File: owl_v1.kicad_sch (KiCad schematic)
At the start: 17 parts, among them SW1 SW_SPDT, U1 STM32F103C8T6, Y1 8MHz, Y2 32k768

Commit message: [feat] Initial routing for the owl PCB
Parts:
- C14, C16: footprint Capacitor_SMD:C_0402_1005Metric -> Capacitor_SMD:C_0603_1608Metric
- L1: footprint Inductor_SMD:L_0402_1005Metric -> Inductor_SMD:L_0603_1608Metric
- SW1: footprint (none) -> Button_Switch_SMD:SW_SPDT_CK_JS102011SAQN
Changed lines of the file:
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@@
 	(wire
 		(pts
+			(xy 46.99 63.5) (xy 48.26 63.5)
+		)
+		(stroke
+			(width 0)
+			(type default)
+		)
+	)
+	(wire
+		(pts
 			(xy 113.03 167.64) (xy 119.38 167.64)
 		)
@@
 	(wire
 		(pts
-			(xy 46.99 63.5) (xy 46.99 67.31)
+			(xy 182.88 104.14) (xy 185.42 104.14)
 		)
 		(stroke
@@
 	(wire
 		(pts
-			(xy 182.88 104.14) (xy 185.42 104.14)
+			(xy 45.72 63.5) (xy 46.99 63.5)
 		)
 		(stroke
@@
 	(wire
 		(pts
-			(xy 48.26 63.5) (xy 46.99 63.5)
+			(xy 64.77 194.31) (xy 71.12 194.31)
 		)
 		(stroke
@@
 	(wire
 		(pts
-			(xy 64.77 194.31) (xy 71.12 194.31)
+			(xy 182.88 78.74) (xy 185.42 78.74)
 		)
 		(stroke
@@
 	(wire
 		(pts
-			(xy 182.88 78.74) (xy 185.42 78.74)
+			(xy 49.53 31.75) (xy 52.07 31.75)
 		)
 		(stroke
@@
 	(wire
 		(pts
-			(xy 49.53 31.75) (xy 52.07 31.75)
+			(xy 238.76 99.06) (xy 242.57 99.06)
 		)
 		(stroke
@@
 	(wire
 		(pts
-			(xy 238.76 99.06) (xy 242.57 99.06)
+			(xy 46.99 63.5) (xy 46.99 67.31)
 		)
 		(stroke
@@
 	(wire
 		(pts
-			(xy 45.72 63.5) (xy 46.99 63.5)
-		)
-		(stroke
-			(width 0)
-			(type default)
-		)
-	)
-	(wire
-		(pts
 			(xy 113.03 171.45) (xy 119.38 171.45)
 		)
@@
 			)
 		)
-		(property "Footprint" "Capacitor_SMD:C_0402_1005Metric"
+		(property "Footprint" "Capacitor_SMD:C_0603_1608Metric"
 			(at 254 35.56 0)
 			(hide yes)
@@
 			)
 		)
-		(property "Footprint" ""
+		(property "Footprint" "Button_Switch_SMD:SW_SPDT_CK_JS102011SAQN"
 			(at 165.1 44.45 0)
 			(hide yes)
@@
 			)
 		)
-		(property "Footprint" "Inductor_SMD:L_0402_1005Metric"
+		(property "Footprint" "Inductor_SMD:L_0603_1608Metric"
 			(at 247.65 31.75 0)
 			(hide yes)
@@
 			)
 		)
-		(property "Footprint" "Capacitor_SMD:C_0402_1005Metric"
+		(property "Footprint" "Capacitor_SMD:C_0603_1608Metric"
 			(at 262.89 35.56 0)
 			(hide yes)

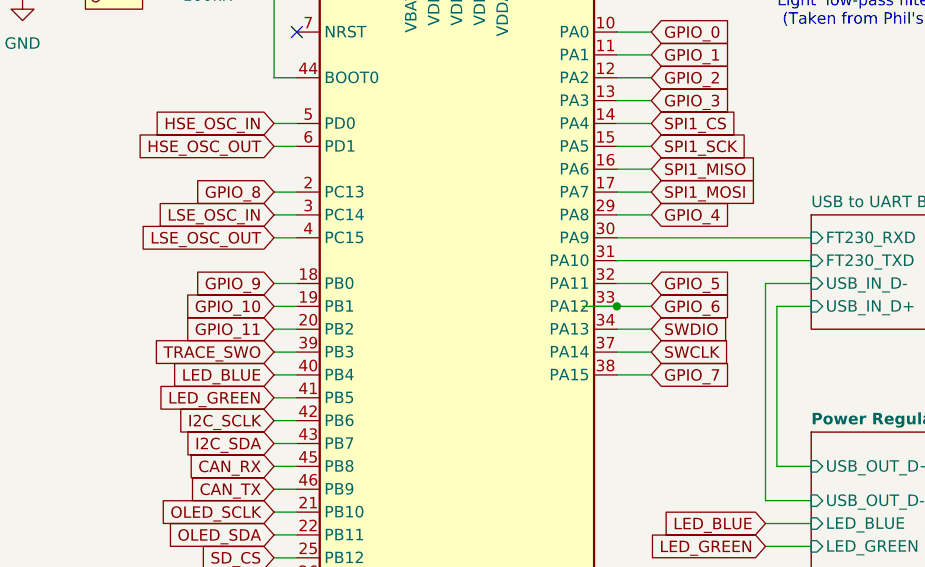
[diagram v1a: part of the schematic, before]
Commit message: [feat] Route most GPIO pins and SWD pins
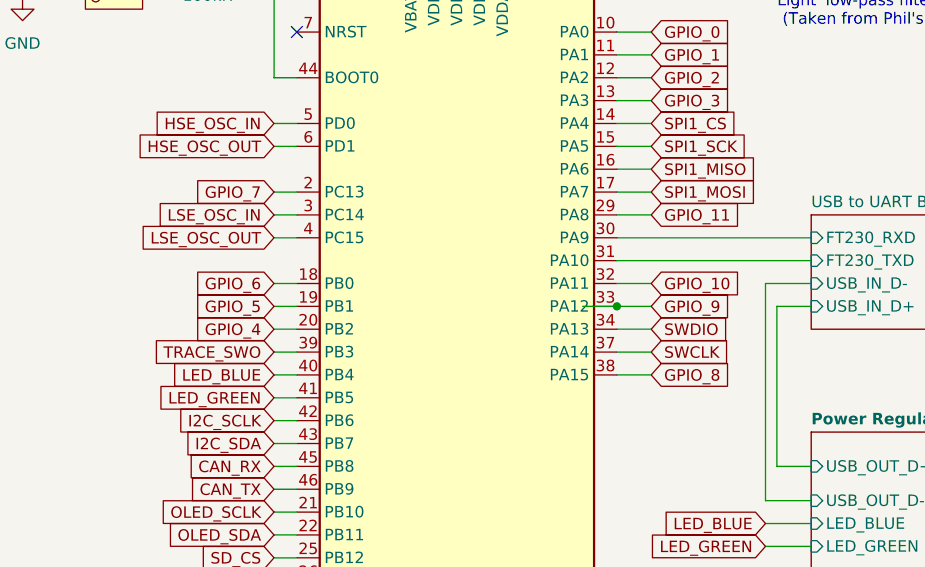
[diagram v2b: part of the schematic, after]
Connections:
- net GPIO_10: now also U1.32 (PA11); no longer U1.19 (PB1)
- net GPIO_11: now also U1.29 (PA8); no longer U1.20 (PB2)
- net GPIO_4: now also U1.20 (PB2); no longer U1.29 (PA8)
- net GPIO_5: now also U1.19 (PB1); no longer U1.32 (PA11)
- net GPIO_6: now also U1.18 (PB0); no longer U1.33 (PA12)
- net GPIO_7: now also U1.2 (PC13); no longer U1.38 (PA15)
- net GPIO_8: now also U1.38 (PA15); no longer U1.2 (PC13)
- net GPIO_9: now also U1.33 (PA12); no longer U1.18 (PB0)

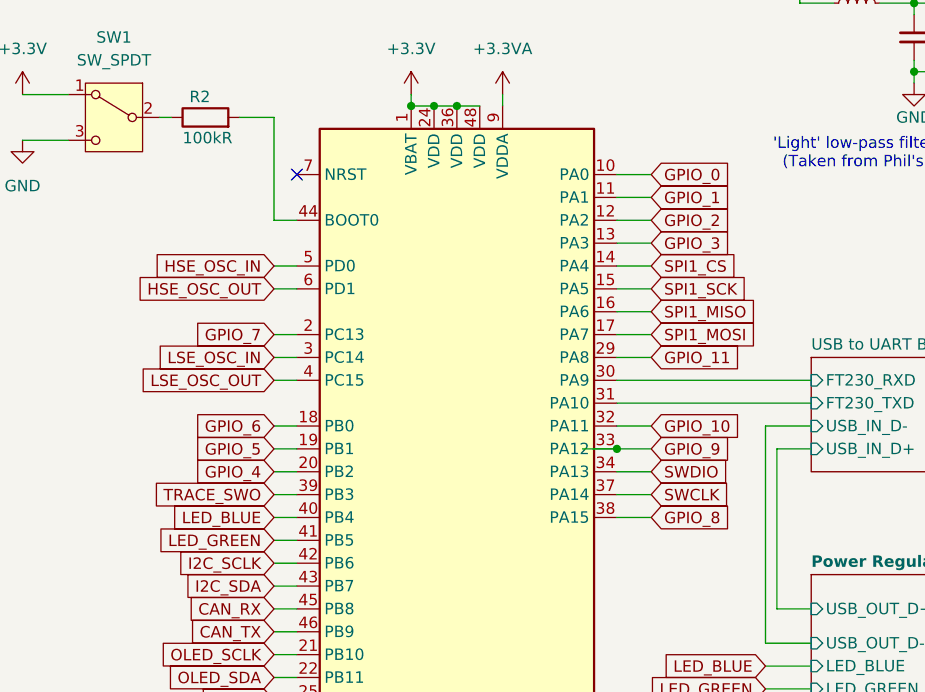
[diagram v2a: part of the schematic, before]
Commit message: [refactor] Expanded the board to get more GPIOs to fit
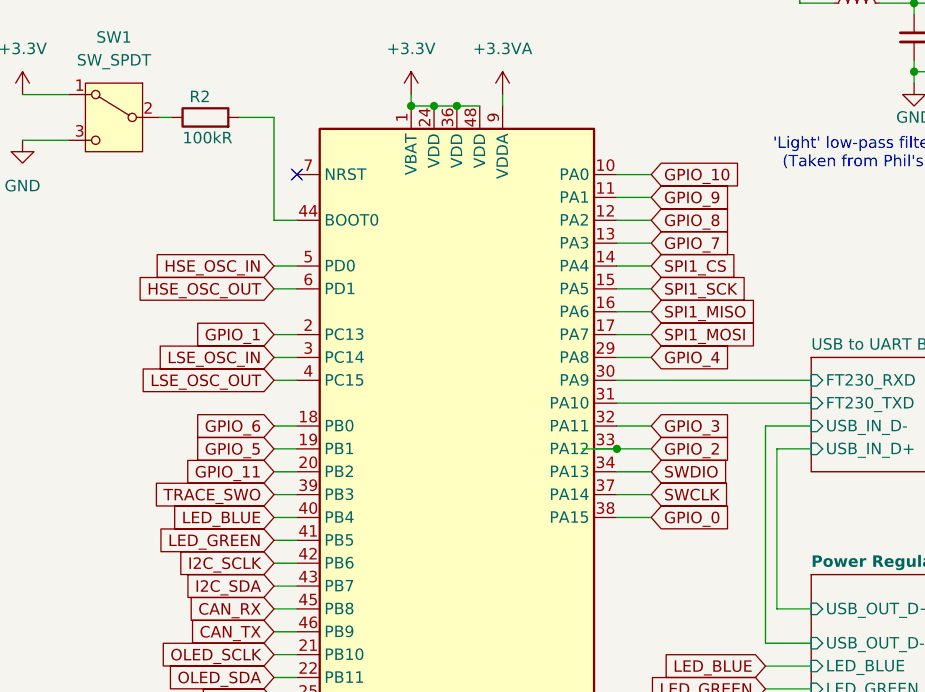
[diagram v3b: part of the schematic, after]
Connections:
- net GPIO_0: now also U1.38 (PA15); no longer U1.10 (PA0)
- net GPIO_1: now also U1.2 (PC13); no longer U1.11 (PA1)
- net GPIO_10: now also U1.10 (PA0); no longer U1.32 (PA11)
- net GPIO_11: now also U1.20 (PB2); no longer U1.29 (PA8)
- net GPIO_2: now also U1.33 (PA12); no longer U1.12 (PA2)
- net GPIO_3: now also U1.32 (PA11); no longer U1.13 (PA3)
- net GPIO_4: now also U1.29 (PA8); no longer U1.20 (PB2)
- net GPIO_7: now also U1.13 (PA3); no longer U1.2 (PC13)
- net GPIO_8: now also U1.12 (PA2); no longer U1.38 (PA15)
- net GPIO_9: now also U1.11 (PA1); no longer U1.33 (PA12)
